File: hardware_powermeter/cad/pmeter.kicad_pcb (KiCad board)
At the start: 4 copper layers, 50 x 16 mm, 59 parts, among them J101 conector magnetico 6 vias, J102 furos da celula, J301 furos da ponte, U101 nPM1100-QDAB, U102 MAX17048G+T10, U201 HOLYIOT-26001-A, U301 ADS1220IRVAR, U302 TPS22916BYFPR, U401 BMA400, U402 TMP117AIDRVR

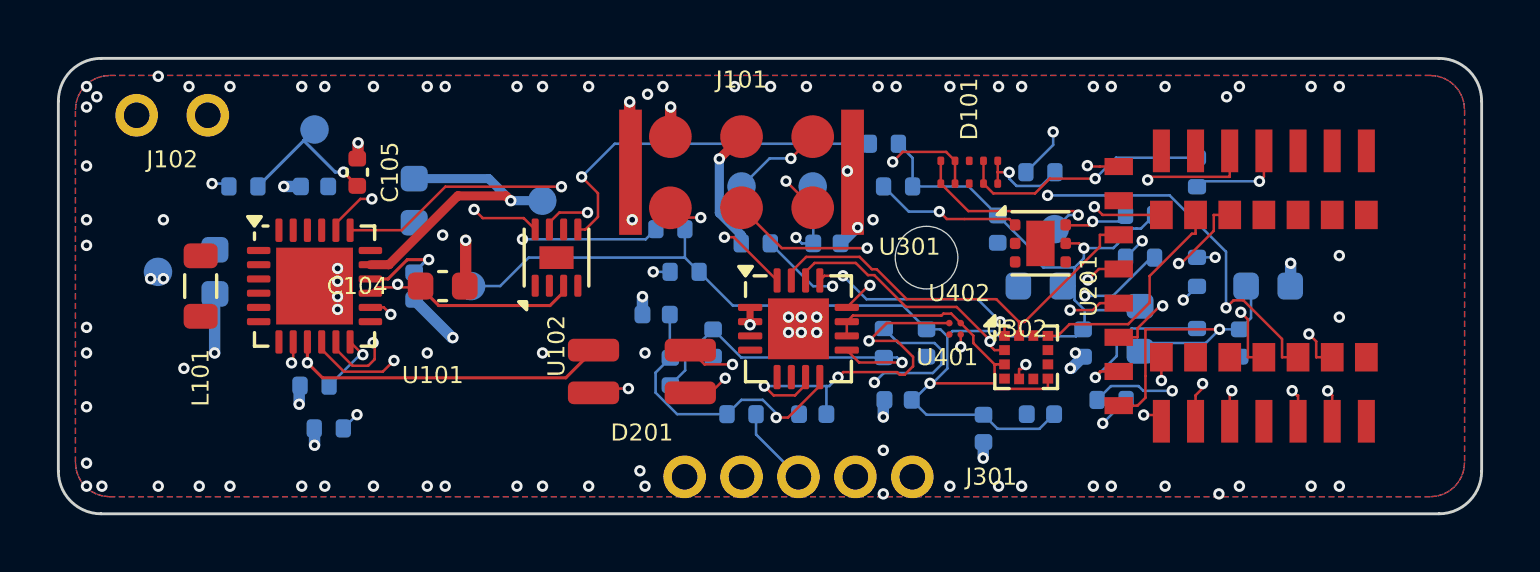
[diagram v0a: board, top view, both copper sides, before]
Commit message: fix(hardware): three faults that made our own passes undo the router's work
Each one was found by measuring the board between the stages instead of only
at the end, and each one had been quietly costing connections.

The 45-degree rewrite was applied to EVERY track, including the router's.
stitch_gnd draws its ground stubs at whatever angle the grid leaves, and
rewrote them into an L of 45 degrees plus a straight run - correct for its
own stubs, and catastrophic for Freerouting's, which produces segments off
45 degrees, as it warns itself ("Invalid traces after autoroute: N traces
not 45 degree"). Each of those became an L that went somewhere else. The
board left Freerouting with ZERO DRC errors and left this file with 123,
among them 59 shorts and 59 mask bridges.

The stitching measured and did nothing. It printed "89 pairs too close" and
wrote the board anyway. Detection without a consequence is not a check, and
this project already decided what the consequence is: what this file drew
comes out, because a stitching via is dispensable item by item - the pad
reaches the plane through the pour of its own face - and a short on a
fabricated board is not.

And GND must stay in the DSN. Taking it out saved the router 32% of its work
(51 of 159 connections) and cost it the SIGHT of 51 pads: with no net, a
ground pad is a netless pad and Freerouting routes straight over it. The way
to see it was a 3V0 track ending at exactly (58.725; 33.0), which is pad 2 of
C203, of GND - 56 shorts from that one decision. The plane is still protected
the right way: In1.Cu is declared (type power) so nothing is routed on it,
and the F.Cu and B.Cu pours still leave the DSN so the router gets bare
copper.

Board: 761 tracks, 90 vias, ZERO DRC errors, 15 connections open against 16.

Also measured and NOT kept: moving U101's own decoupling back to the front.
Freerouting liked it - 7 unrouted, its best ever - but the board came out
with 119 to 194 DRC errors that stayed unexplained across thr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
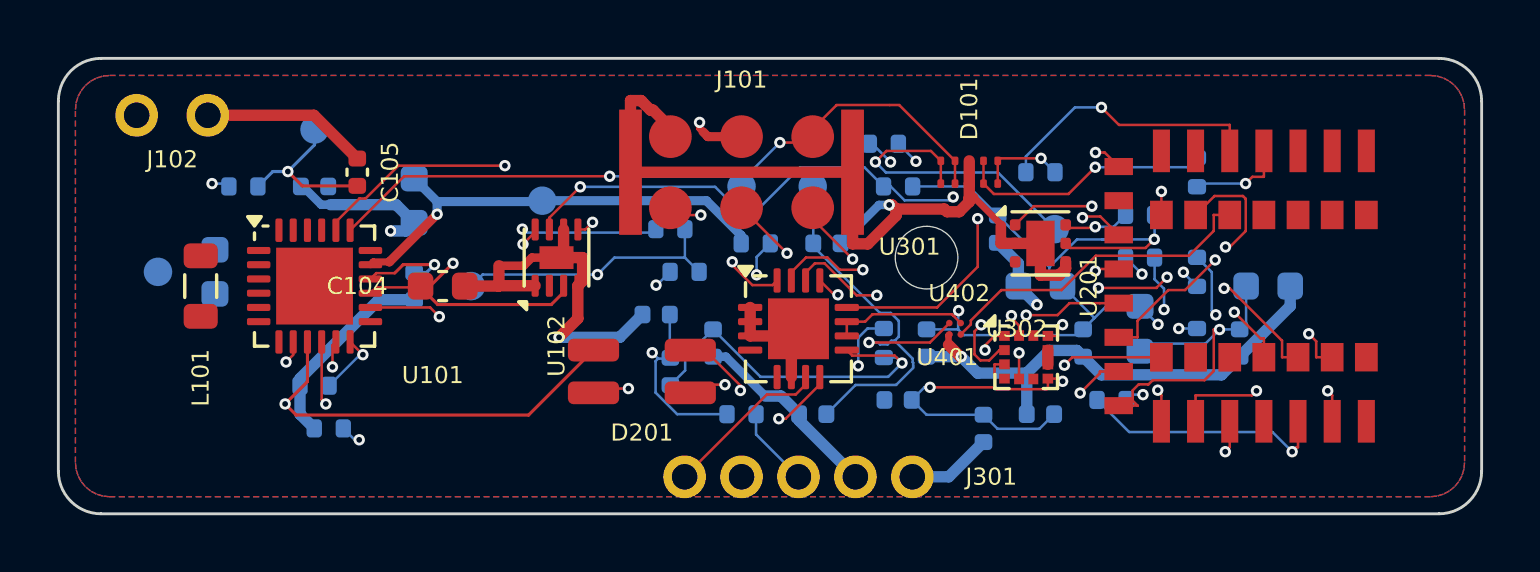
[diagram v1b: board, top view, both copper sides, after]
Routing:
- net GND: track 16.2 -> 97.1 mm, vias 105 -> 5
- net 3V0: track 63.1 -> 83.3 mm, vias 2 -> 7
- net LED_KR: track 42.4 -> 26.0 mm
- net EXC_EN: track 25.4 -> 11.6 mm, vias 2 -> 0
- net GAUGE_ALRT: track 40.7 -> 32.3 mm, vias 2 -> 3
- net UART_TX: track 54.9 -> 62.7 mm
- net UART_RX: track 49.6 -> 57.2 mm, vias 4 -> 3
- net SWCLK_J: track 12.6 -> 19.5 mm
- net I2C_SCL: track 41.9 -> 35.3 mm
- net LED_KG: track 18.9 -> 25.2 mm
- net SHPHLD: track 17.2 -> 11.6 mm
- net VBUS: track 23.2 -> 28.5 mm
- net VSYS: track 20.4 -> 25.3 mm
- net 3V0_EXC: track 25.5 -> 30.3 mm, vias 4 -> 1
- net IMU_CS: track 7.88 -> 12.6 mm, vias 0 -> 4
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
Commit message: feat(hardware): one connection open, and the ground stitched before the router
From 21 connections without copper yesterday to ONE, with zero DRC errors,
and the thing that did it was the owner's instruction: close them one at a
time instead of running everything at once and throwing the result away when
it got worse.

The order was wrong. The ground stitching ran AFTER the router, and on a
board that is already full a via has nowhere to land: of the 112 items it
placed, 105 were too close to the router's copper and the cleanup removed
them - which also removed the edge stitching, and GN2 said so ("only 1
ground via within 3 mm of the edge: there is no stitching"). A plane with no
stitching is not a plane at 2.4 GHz. Stitched FIRST, on the bare board where
everything fits, it keeps 46 pads with a via of their own, 40 vias along the
edge and 43 in the mesh, and the router goes round them. That reordering
alone took the board from 15 open to 2.

This only became possible after learning that the DSN CAN carry copper. Two
earlier attempts to put copper in before routing produced a zero-byte .ses
and the conclusion was "the DSN must be bare" - it was wrong. What broke was
Freerouting's GUI crashing on our pour; headless and without the pour, it
reads a board with copper and writes the session normally.

Then the refining: route, measure, remove whatever the FABRICATOR rejects,
measure again, repeat. limpar_curtos.py removes by UUID only the tracks the
KiCad DRC calls a short - pads and vias stay, because a pad is the part and a
via may be the only link between faces. And only below 0.0889 mm, the
fabricator's own minimum: our geometric check is deliberately stricter, and
removing everything it flags is what had cost the stitching.

fechar_ultimas.py takes what is left one by one, by what it is: ends on
different layers get a via where both reach, ends on the same layer get a
stub, and an end that is the POUR gets a via beside the pad - the DRC gives a
point inside the re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
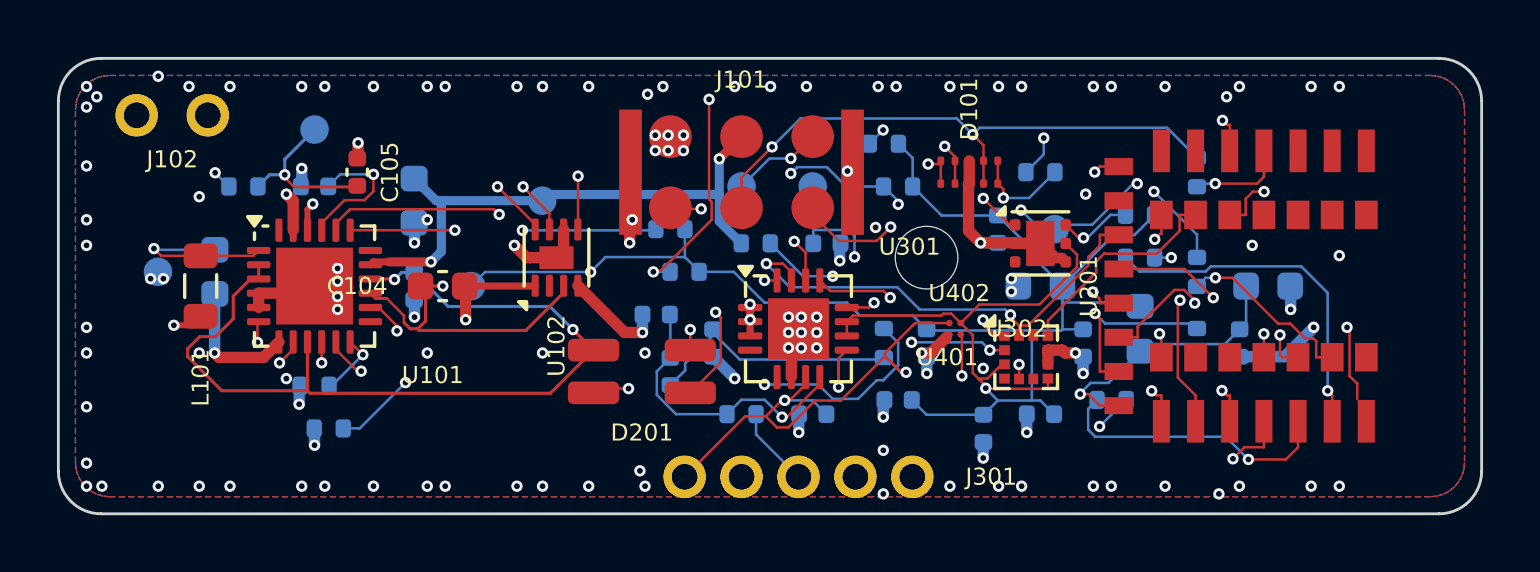
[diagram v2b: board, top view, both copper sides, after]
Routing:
- net GND: track 97.1 -> 48.4 mm, vias 5 -> 129
- net SHPACT: track 0.00 -> 42.3 mm, vias 0 -> 2
- net CHG_N: track 20.7 -> 55.3 mm, vias 2 -> 4
- net UART_TX: track 62.7 -> 48.8 mm, vias 4 -> 6
- net 3V0: track 83.3 -> 96.1 mm, vias 7 -> 3
- net BUCK_SW: track 0.00 -> 12.7 mm, vias 0 -> 2
- net UART_RX: track 57.2 -> 45.1 mm, vias 3 -> 4
- net IMU_INT1: track 6.87 -> 18.8 mm
- net EXC_EN: track 11.6 -> 22.5 mm, vias 0 -> 2
- net SPI_MOSI: track 17.1 -> 26.3 mm, vias 3 -> 4
- net VBUS: track 28.5 -> 20.0 mm
- net SWCLK_J: track 19.5 -> 11.5 mm
- net I2C_SDA: track 36.0 -> 42.0 mm
- net VSYS: track 25.3 -> 31.0 mm
- net DEC: track 0.00 -> 4.89 mm, vias 0 -> 1
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
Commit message: feat(hardware): the board is routed - 0 DRC errors, 0 connections open
838 tracks, 221 vias, zero DRC errors and ZERO unconnected items, against 21
open yesterday. The 52 violations left are the known warnings: 44 library
footprint mismatches, because this project's footprints are generated, 7
library issues and one silkscreen at the edge.

RT1 passes for the first time. GN1 says all 49 surface ground pads are
connected, 42 of them by a via of their own to the inner plane; GN2 counts 73
vias along the edge with a largest gap of 3.0 mm. The board's dry run goes
from 14 rules met and 6 violated to 16 and 4.

What closed it was the ORDER, not the tool, and it was the owner's call: one
at a time instead of everything at once. The ground stitching moved to BEFORE
the router, on the bare board where every via fits - run afterwards, 105 of
its 112 items were too close to the router's copper and were removed, taking
the edge stitching with them. That reordering alone took the board from 15
open to 2.

It only became possible after learning the DSN CAN carry copper. Two earlier
attempts produced a zero-byte .ses and the conclusion then - "the DSN must be
bare" - was wrong: what broke was Freerouting's GUI crashing on our pour.

Then refining one pass at a time: route, measure, remove what the FABRICATOR
rejects, measure again. limpar_curtos.py deletes by UUID only the tracks the
KiCad DRC calls a short, and only below 0.0889 mm, because our own check is
deliberately stricter and removing everything it flags is what had cost the
stitching.

fechar_ultimas.py takes what is left one by one, by what each one is: a via
when the ends are on different layers, a stub when they are on the same, and
a via beside the pad when the other end is the pour. The stub starts at the
pad's EDGE and may TURN - straight, L, or L of 45 degrees. That mattered: the
module's two ground pads sit at x 45.95 and the antenna's exclusion zone
starts at 45.70, so their centres are inside it and their left 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
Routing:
- net GND: track 48.4 -> 51.8 mm
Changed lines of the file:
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@@
+	)
+	(segment
+		(start 70.63 36.97)
+		(end 70.63 36.43)
+		(width 0.09)
+		(layer "F.Cu")
+		(net 11)
+	)
+	(segment
+		(start 47.86 26.44)
+		(end 47.86 29.95)
+		(width 0.09)
+		(layer "F.Cu")
+		(net 11)
+	)
+	(segment
+		(start 33.25 35.2181)
+		(end 32.7698 35.6983)
+		(width 0.09)
+		(layer "F.Cu")
+		(net 11)
 	)
 	(segment
@@
 	)
 	(segment
-		(start 70.63 36.97)
-		(end 70.63 36.43)
-		(width 0.09)
-		(layer "F.Cu")
-		(net 11)
-	)
-	(segment
-		(start 47.86 26.44)
-		(end 47.86 29.95)
-		(width 0.09)
-		(layer "F.Cu")
-		(net 11)
-	)
-	(segment
-		(start 33.25 35.2181)
-		(end 32.7698 35.6983)
-		(width 0.09)
-		(layer "F.Cu")
-		(net 11)
-	)
-	(segment
 		(start 70.63 36.43)
 		(end 70.36 36.16)
@@
 	)
 	(segment
+		(start 35.1714 36.6182)
+		(end 32.8404 36.6182)
+		(width 0.09)
+		(layer "In2.Cu")
+		(net 11)
+	)
+	(segment
 		(start 66.04 26.71)
 		(end 48.13 26.71)
@@
 	)
 	(segment
-		(start 35.1714 36.6182)
-		(end 32.8404 36.6182)
+		(start 66.49 27.16)
+		(end 66.04 26.71)
 		(width 0.09)
 		(layer "In2.Cu")
@@
 		(start 45.9017 32.5)
 		(end 41.4431 36.9586)
-		(width 0.09)
-		(layer "In2.Cu")
-		(net 11)
-	)
-	(segment
-		(start 66.49 27.16)
-		(end 66.04 26.71)
 		(width 0.09)
 		(layer "In2.Cu")
@@
 	)
 	(segment
+		(start 70.63 34.18)
+		(end 70.27 33.82)
+		(width 0.09)
+		(layer "F.Cu")
+		(net 16)
+	)
+	(segment
 		(start 41.02 31.57)
 		(end 41.4499 31.9999)
@@
 		(end 39.31 34.18)
 		(width 0.4)
+		(layer "F.Cu")
+		(net 16)
+	)
+	(segment
+		(start 70.27 33.82)
+		(end 68.29 33.82)
+		(width 0.09)
 		(layer "F.Cu")
 		(net 16)
@@
 	)
 	(segment
+		(start 70.63 34.99)
+		(end 70.63 34.18)
+		(width 0.09)
+		(layer "F.Cu")
+		(net 16)
+	)
+	(segment
 		(start 32.0375 33.25)
 		(end 32.0375 33.75)
@@
 		(layer "F.Cu")
 		(net 16)
+	)
+	(segment
+		(start 70.54 34.99)
+		(end 70.63 34.99)
+		(width 0.09)
+		(layer "F.Cu")
+		(net 16)

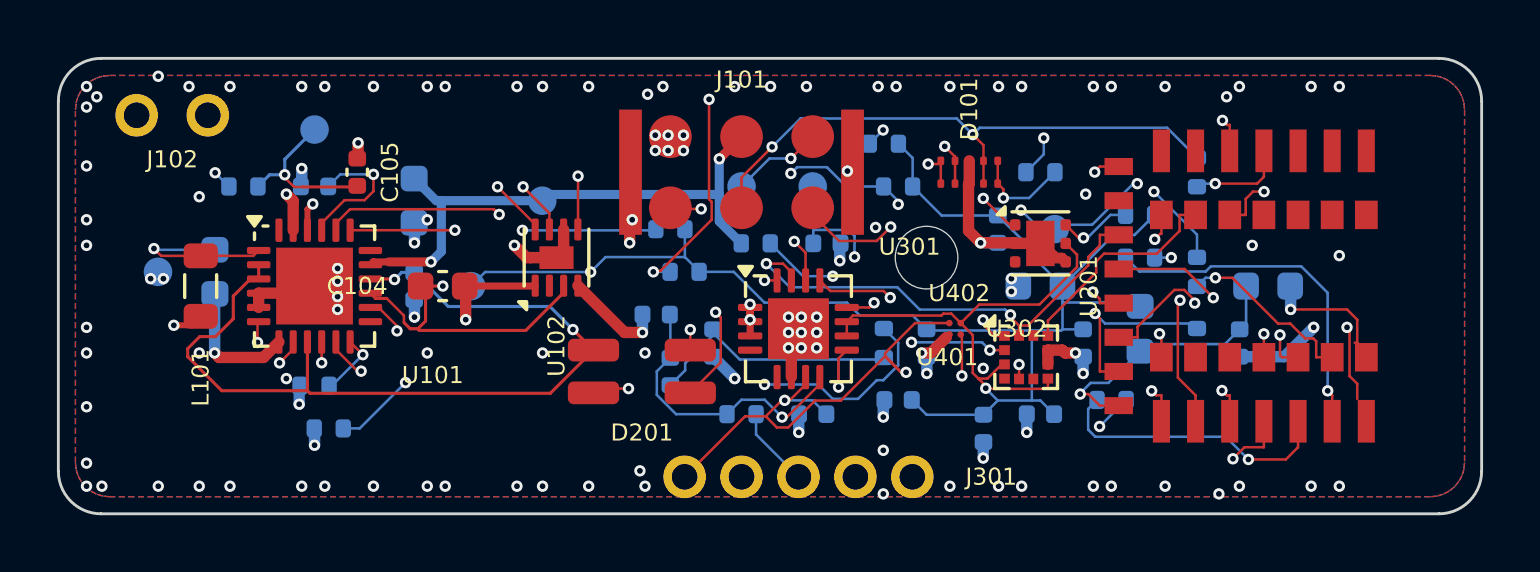
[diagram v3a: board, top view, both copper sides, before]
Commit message: feat(hardware): the cell enters by connector, and the board generates again
The owner asked for the cell to arrive with its two wires AND its plug, and
for the board's receptacle to be the angled one - mouth parallel to the board,
not the vertical kind. Both are done, and the way there uncovered two defects
that had nothing to do with connectors.

THE CONNECTOR. J102 was two plated holes for hand-soldered wire since
2026-09-26, and the argument for that was good: it took the tallest part off
the board, 2.90 mm, which set the lid's ceiling by itself. What it did not see
is that the cell you BUY arrives with a plug, so holes mean cutting it off and
soldering bare 30 AWG inside a 20 mm box, with the cell no longer replaceable.

The series was measured, not guessed. All three were placed on the board and
the pod measured with each, from the KiCad library's 3D models:

  PH 2,0  S2B-PH-SM4-TB   4,85 mm   5,9 x 7,6   pod 9,70   17,7 g  24 of 32
  GH 1,25 SM02B-GHS-TB    4,24 mm   5,8 x 5,0   pod 9,04      -        -
  SH 1,0  SM02B-SRSS-TB   2,90 mm   4,3 x 4,0   pod 7,70   14,5 g  30 of 32

PH is what pouch cells ship with - confirmed on three documented parts - and
it was tried first. Its bill does not close: it would force the magnetic
connector up to 5,35 mm (the reserved place is 3,2, and with the ceiling at
5,15 its face would sit 2,0 mm BELOW the lid - the charging port would stop
existing), widen the channel by 1,8 mm for the plug, leave the screw heads
1,1 mm over the height target, take the blind screw hole to 5,5:1, and put the
glue-plus-pod stack at 10,2 mm against the 10,0 of frame clearance the project
reserved. SH costs one line on the cell's order instead: pouch makers sell the
connector as an option.

THE CABLE CUT the owner asked not to forget was already there - 3,4 mm through
the ribs and the floor - but it had been cut for two bare wires. With a plug,
PD21 and PD32 caught that the left screw's boss stood right in front of it,
and that the plug had 0,0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
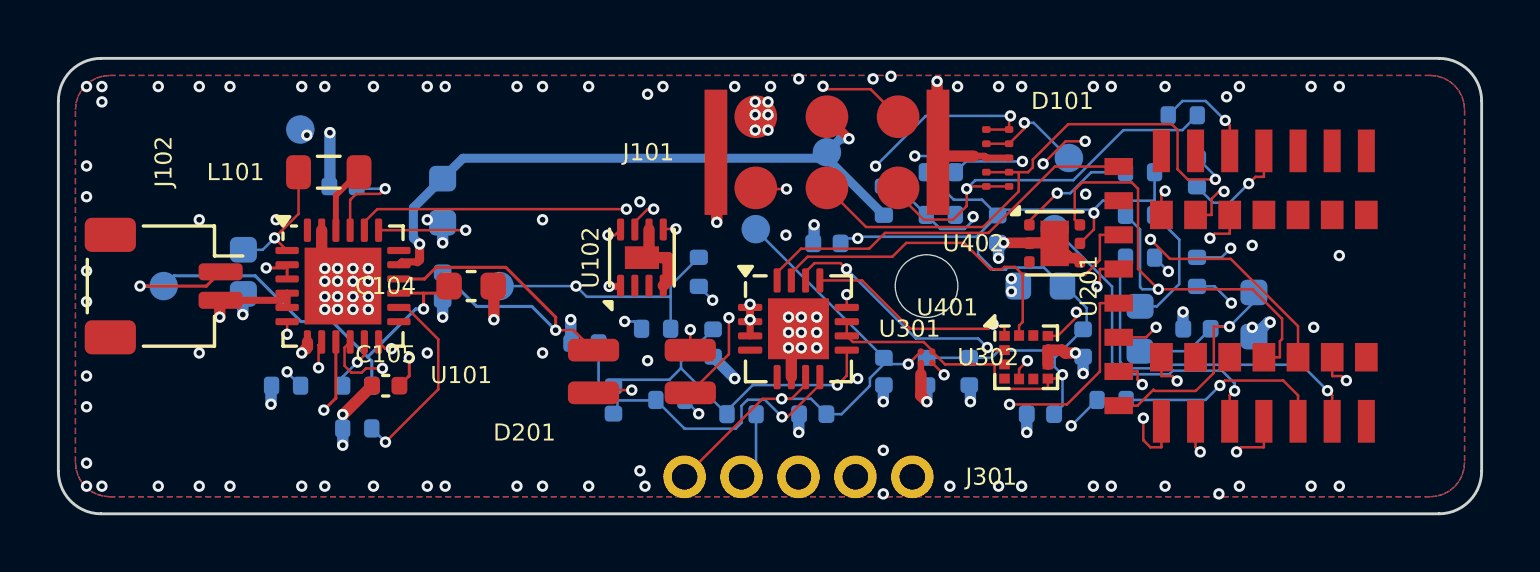
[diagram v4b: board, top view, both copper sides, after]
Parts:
- J102: footprint pmeter:Furos_Celula_2x1.5mm_P2.5mm -> Connector_JST:JST_SH_SM02B-SRSS-TB_1x02-1MP_P1.00mm_Horizontal
- moved TP202 11.5 mm to (60.5, 28.5)
- moved TP101 10.1 mm to (52.0, 28.3)
- moved R110 10.1 mm to (56.0, 30.5), turned to 180 degrees
- moved R205 8.51 mm to (63.0, 29.0)
- moved R106 8.06 mm to (35.5, 36.5)
- moved TP102 7.64 mm to (28.7, 33.0)
- moved C105 7.57 mm to (36.5, 36.5), turned to 180 degrees
- moved TP104 7.07 mm to (33.5, 27.5)
- moved L101 6.02 mm to (34.5, 29.0), turned to 180 degrees
- moved J102 6.01 mm to (28.7, 33.0), turned to -90 degrees
- moved R301 5.59 mm to (49.0, 37.5), turned to 0 degrees
- moved R108 5.39 mm to (64.5, 27.0)
- moved C306 4.95 mm to (52.0, 31.5), turned to 0 degrees
- moved C307 4.92 mm to (54.0, 36.0), turned to 90 degrees
- moved R109 4.74 mm to (54.0, 30.0), turned to -90 degrees
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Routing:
- net CHG_N: track 55.3 -> 13.4 mm, vias 4 -> 2
- net 3V0: track 96.1 -> 82.2 mm, vias 3 -> 5
- net IMU_INT1: track 18.8 -> 5.90 mm
- net 3V0_EXC: track 31.2 -> 18.8 mm, vias 3 -> 2
- net GAUGE_ALRT: track 33.7 -> 23.3 mm, vias 3 -> 4
- net BUCK_SW: track 12.7 -> 2.37 mm, vias 2 -> 0
- net GND: track 51.8 -> 42.2 mm, vias 129 -> 144
- net SHPHLD: track 11.2 -> 1.85 mm, vias 2 -> 1
- net VBAT: track 30.6 -> 21.6 mm, vias 2 -> 3
- net ERR_N: track 43.7 -> 34.7 mm
- net UART_TX: track 48.8 -> 57.2 mm, vias 6 -> 5
- net BR_SP: track 10.5 -> 2.41 mm, vias 1 -> 0
- net UART_RX: track 45.1 -> 52.7 mm
- net SPI_MOSI: track 26.3 -> 19.5 mm, vias 4 -> 3
- net SWDCLK: track 9.23 -> 3.63 mm, vias 2 -> 1
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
